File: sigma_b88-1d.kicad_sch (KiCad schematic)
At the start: 32 parts, among them IC11 74LS259, IC18 74LS259, IC27 74LS00, IC3 74LS259, IC31 74LS138, IC33 74LS07, IC34 74LS138, IC39 74LS367, IC4 74LS259, IC40 74LS138, IC43 74HC245, IC44 74LS139, IC45 74HC373, IC46 74HC374, IC55 74HC245, IC56 74LS139, IC57 74LS32, IC58 74LS259, IC63 74HC74, IC64 74HC373, IC73 TC551001BPL, IC74 TC551001BPL, IC75 74LS139, IC86 27C040, IC87 27C040, IC96 27C040, IC97 27C040, U1 74LS139, U2 74LS07, U3 74LS139, U4 74LS139

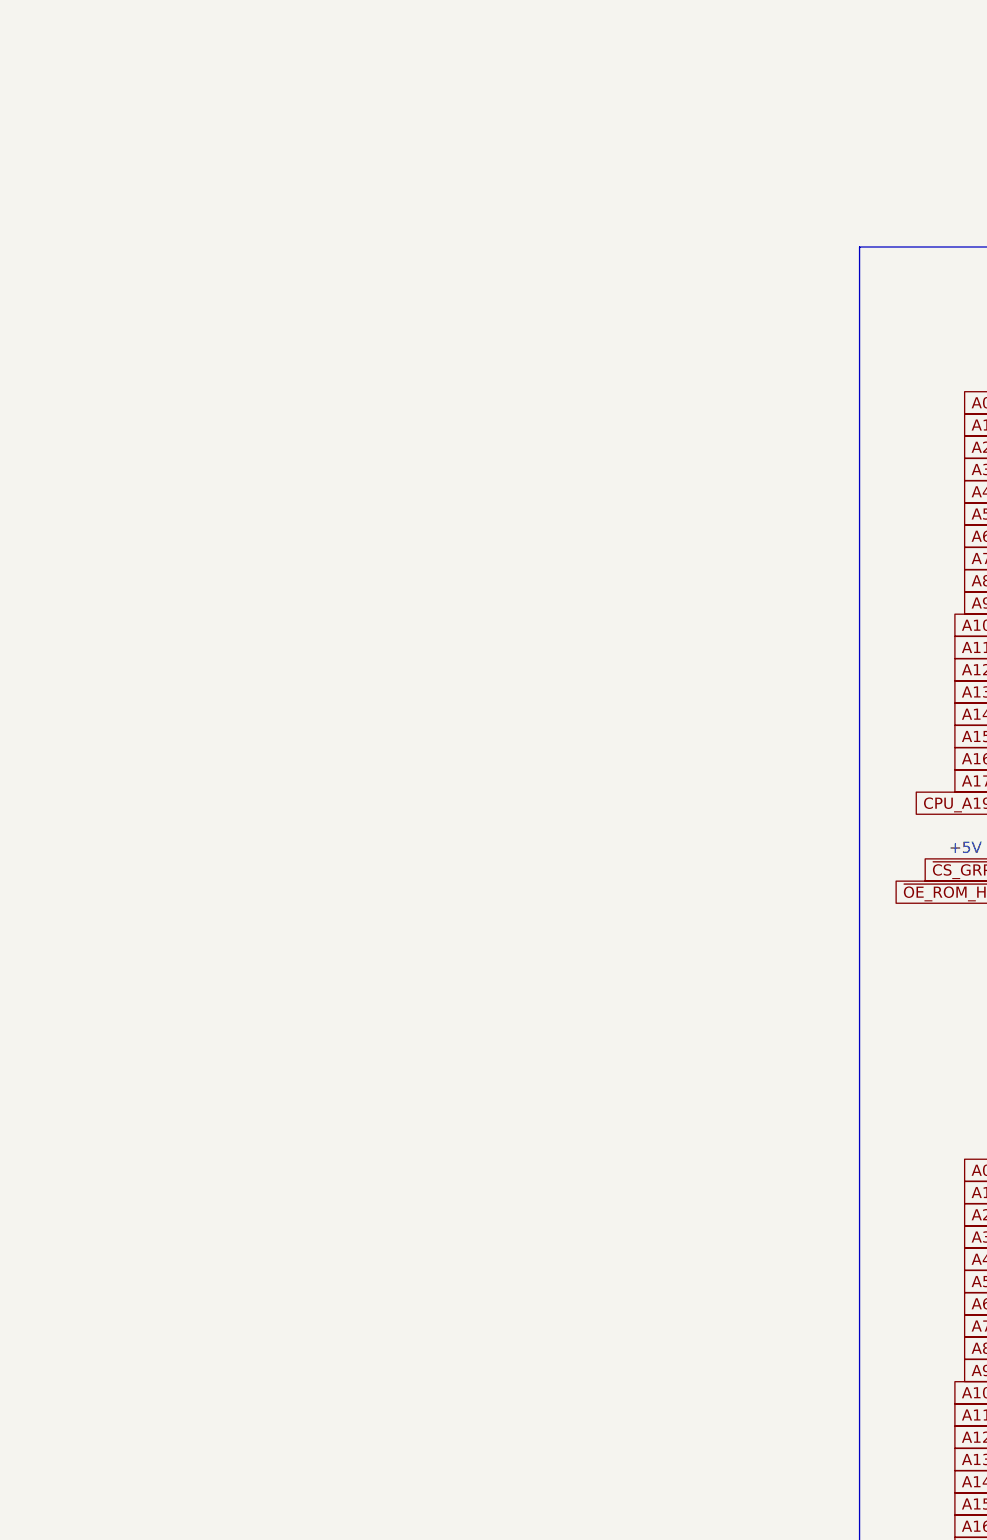
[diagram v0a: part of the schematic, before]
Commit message: Add CPU & some progz
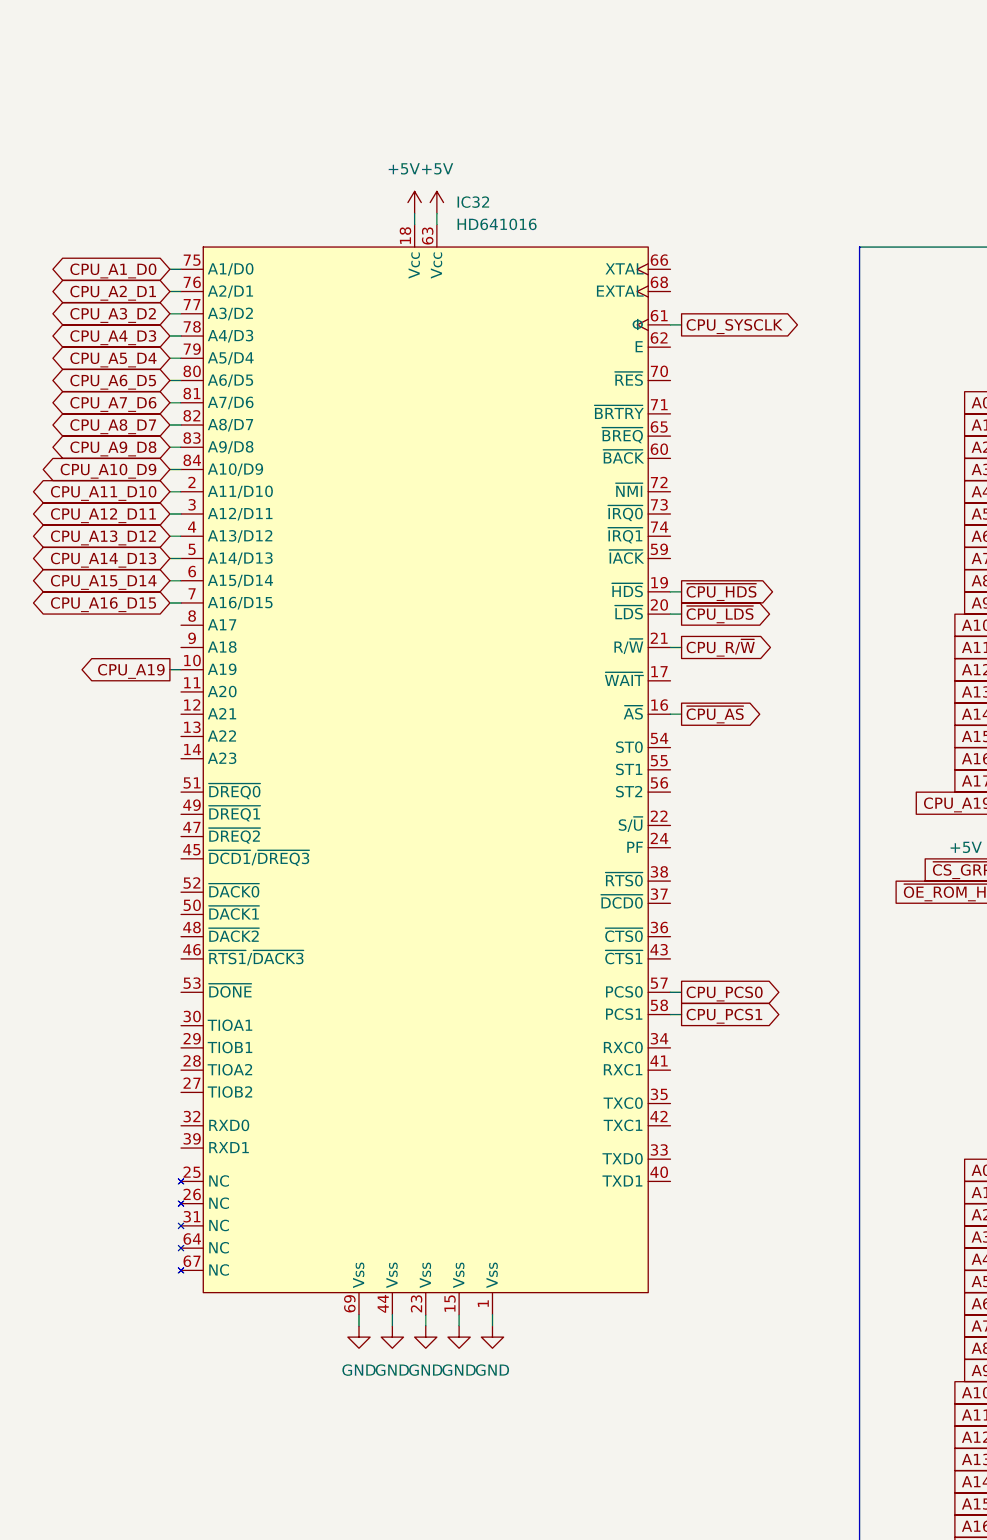
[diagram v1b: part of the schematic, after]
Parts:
- added IC32: HD641016, symbol Custom_parts:HD641016
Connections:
- net +5V: now also IC32.18 (Vcc), IC32.63 (Vcc)
- net CPU_A10_D9: now also IC32.84 (A10/D9)
- net CPU_A11_D10: now also IC32.2 (A11/D10)
- net CPU_A12_D11: now also IC32.3 (A12/D11)
- net CPU_A13_D12: now also IC32.4 (A13/D12)
- net CPU_A14_D13: now also IC32.5 (A14/D13)
- net CPU_A15_D14: now also IC32.6 (A15/D14)
- net CPU_A16_D15: now also IC32.7 (A16/D15)
- net CPU_A19: now also IC32.10 (A19)
- net CPU_A1_D0: now also IC32.75 (A1/D0)
- net CPU_A2_D1: now also IC32.76 (A2/D1)
- net CPU_A3_D2: now also IC32.77 (A3/D2)
- net CPU_A4_D3: now also IC32.78 (A4/D3)
- net CPU_A5_D4: now also IC32.79 (A5/D4)
- net CPU_A6_D5: now also IC32.80 (A6/D5)
- net CPU_A7_D6: now also IC32.81 (A7/D6)
- net CPU_A8_D7: now also IC32.82 (A8/D7)
- net CPU_A9_D8: now also IC32.83 (A9/D8)
- net CPU_PCS0: now also IC32.57 (PCS0)
- net CPU_PCS1: now also IC32.58 (PCS1)
- net CPU_R/~{W}: now also IC32.21 (R/~{W})
- net CPU_SYSCLK: now also IC32.61 (Φ)
- net GND: now also IC32.1 (Vss), IC32.15 (Vss), IC32.23 (Vss), IC32.44 (Vss), IC32.69 (Vss)
- net ~{CPU_AS}: now also IC32.16 (~{AS})
- net ~{CPU_HDS}: now also IC32.19 (~{HDS})
- net ~{CPU_LDS}: now also IC32.20 (~{LDS})
